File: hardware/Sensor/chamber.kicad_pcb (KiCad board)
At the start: 2 copper layers, 45 x 30 mm, 30 parts, among them J1 Power, J2 Chamber, J3 Output, Q1 Q_NJFET_DGS, Q2 BC546, Q3 BC327, U1 LMC6082

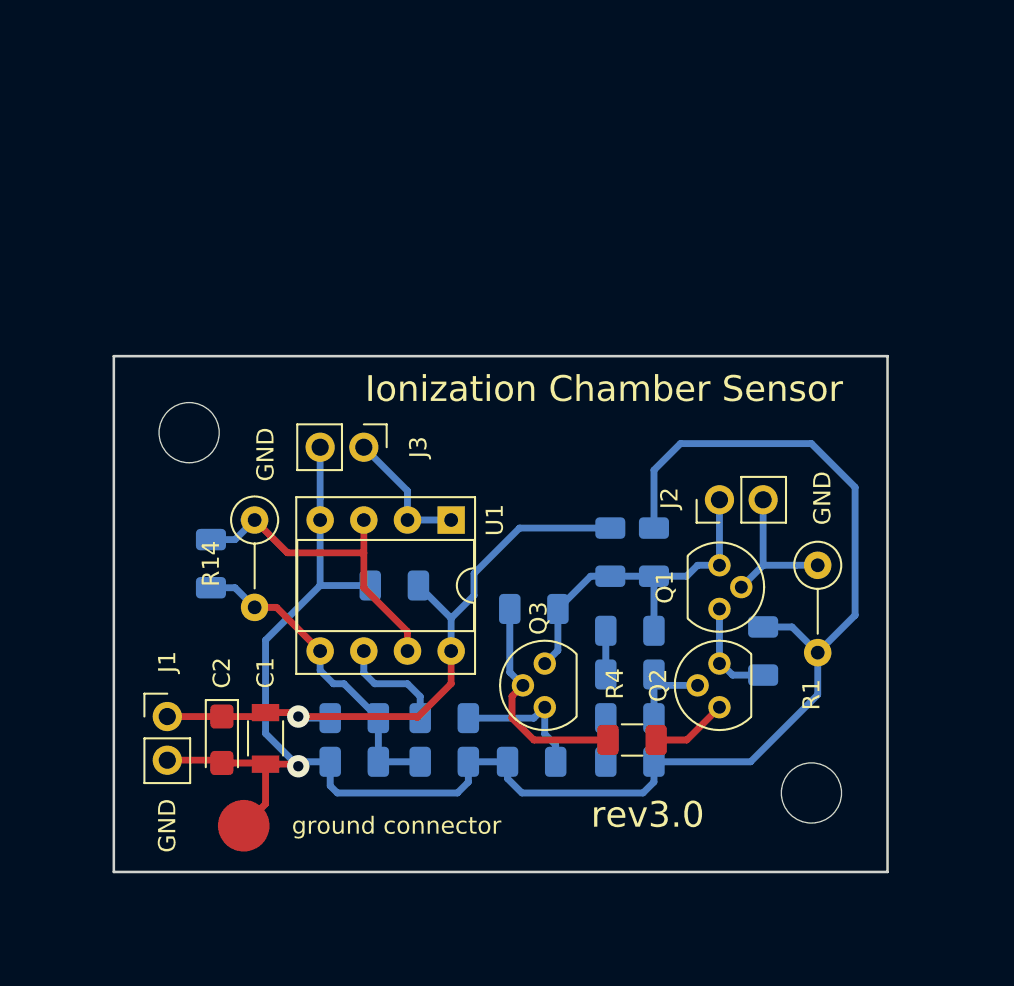
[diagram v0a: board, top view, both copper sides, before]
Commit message: fixed footprints
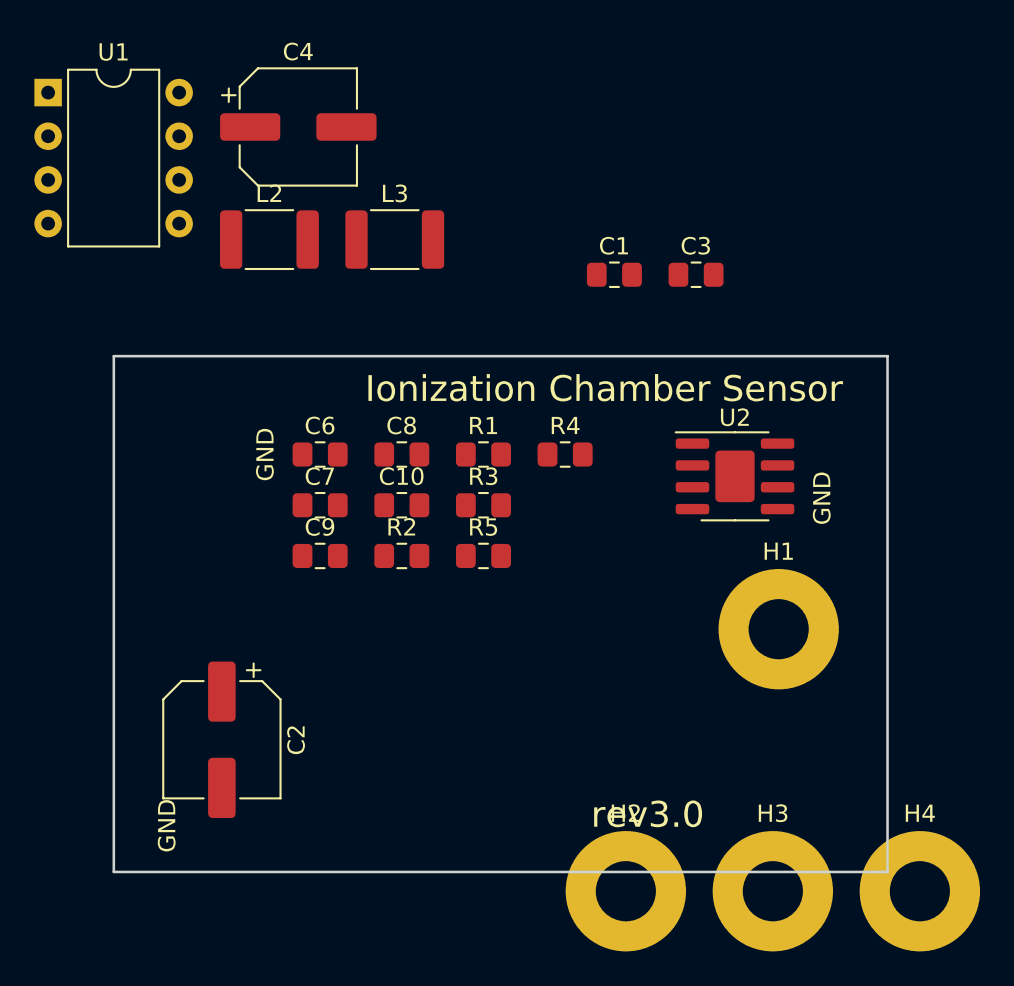
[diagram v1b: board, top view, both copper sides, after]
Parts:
- removed C5: 100n, Capacitor_SMD:C_1206_3216Metric
- removed J1: Power, Connector_PinHeader_2.54mm:PinHeader_1x02_P2.54mm_Vertical
- removed J2: Chamber, Connector_PinHeader_2.54mm:PinHeader_1x02_P2.54mm_Vertical
- removed J3: Output, Connector_PinHeader_2.54mm:PinHeader_1x02_P2.54mm_Vertical
- removed Q1: Q_NJFET_DGS, Package_TO_SOT_THT:TO-92
- removed Q2: BC546, Package_TO_SOT_THT:TO-92
- removed Q3: BC327, Package_TO_SOT_THT:TO-92
- removed R10: 1k, Resistor_SMD:R_1206_3216Metric
- removed R11: 47k, Resistor_SMD:R_1206_3216Metric
- removed R12, R13: R, Resistor_SMD:R_1206_3216Metric
- removed R14: 4M7, Resistor_THT:R_Axial_DIN0207_L6.3mm_D2.5mm_P5.08mm_Vertical
- removed R6, R7: 0R, Resistor_SMD:R_1206_3216Metric
- removed R8: 150k, Resistor_SMD:R_1206_3216Metric
- removed R9: 220k, Resistor_SMD:R_1206_3216Metric
- removed REF** (x2): MountingHole_3.5mm, Mounting_Holes:MountingHole_3.5mm
- removed ground connector: Measurement_Point_Round-SMD-Pad_Big, Measurement_Points:Measurement_Point_Round-SMD-Pad_Big
- added C10: 100n, Capacitor_SMD:C_0805_2012Metric_Pad1.15x1.40mm_HandSolder, F.Cu at (131.8, 48.7)
- added C7: 100n, Capacitor_SMD:C_0805_2012Metric_Pad1.15x1.40mm_HandSolder, F.Cu at (127.0, 48.7)
- added C8: 100n, Capacitor_SMD:C_0805_2012Metric_Pad1.15x1.40mm_HandSolder, F.Cu at (131.8, 45.7)
- added C9: 100n, Capacitor_SMD:C_0805_2012Metric_Pad1.15x1.40mm_HandSolder, F.Cu at (127.0, 51.6)
- added H1: top left, MountingHole:MountingHole_3.5mm_Pad, F.Cu at (153.7, 55.9)
- added H2: bottom left, MountingHole:MountingHole_3.5mm_Pad, F.Cu at (144.8, 71.1)
- added H3: top right, MountingHole:MountingHole_3.5mm_Pad, F.Cu at (153.3, 71.1)
- added H4: bottom right, MountingHole:MountingHole_3.5mm_Pad, F.Cu at (161.9, 71.1)
- added L2: u68, Inductor_SMD:L_1812_4532Metric_Pad1.30x3.40mm_HandSolder, F.Cu at (124.0, 33.2)
- added L3: u68, Inductor_SMD:L_1812_4532Metric_Pad1.30x3.40mm_HandSolder, F.Cu at (131.3, 33.2)
- added U2: LM358, Package_SO:SOIC-8-1EP_3.9x4.9mm_P1.27mm_EP2.29x3mm, F.Cu at (151.1, 47.0)
- C1: value 100n -> 2p2; footprint Capacitors_SMD:C_1206 -> Capacitor_SMD:C_0805_2012Metric_Pad1.15x1.40mm_HandSolder
- C2: footprint Capacitor_Tantalum_SMD:CP_EIA-3216-18_Kemet-A -> Capacitor_SMD:CP_Elec_6.3x5.4
- C3: value 100n -> C; footprint Capacitor_SMD:C_1206_3216Metric -> Capacitor_SMD:C_0805_2012Metric_Pad1.15x1.40mm_HandSolder; moved to F.Cu
- C4: value C -> 100u/16V; footprint Capacitor_SMD:C_1206_3216Metric -> Capacitor_SMD:CP_Elec_6.3x5.4; moved to F.Cu
- C6: footprint Capacitor_SMD:C_1206_3216Metric -> Capacitor_SMD:C_0805_2012Metric_Pad1.15x1.40mm_HandSolder; moved to F.Cu
- R1: value 1G -> 4*100G; footprint Resistor_THT:R_Axial_DIN0207_L6.3mm_D2.5mm_P5.08mm_Vertical -> Resistor_SMD:R_0805_2012Metric_Pad1.15x1.40mm_HandSolder
- R2: value 270k -> R; footprint Resistor_SMD:R_1206_3216Metric -> Resistor_SMD:R_0805_2012Metric_Pad1.15x1.40mm_HandSolder; moved to F.Cu
- R3: value 100k -> R; footprint Resistor_SMD:R_1206_3216Metric -> Resistor_SMD:R_0805_2012Metric_Pad1.15x1.40mm_HandSolder; moved to F.Cu
- R4: value 270k -> R; footprint Resistor_SMD:R_1206_3216Metric -> Resistor_SMD:R_0805_2012Metric_Pad1.15x1.40mm_HandSolder
- R5: value 47k -> R; footprint Resistor_SMD:R_1206_3216Metric -> Resistor_SMD:R_0805_2012Metric_Pad1.15x1.40mm_HandSolder; moved to F.Cu
- U1: value LMC6082 -> LMC662; footprint Housings_DIP:DIP-8_W7.62mm_Socket -> Package_DIP:DIP-8_W7.62mm
- moved C4 37.9 mm to (125.7, 26.7)
- moved U1 34.2 mm to (111.2, 24.7), turned to 0 degrees
- moved C1 33.7 mm to (144.1, 35.3), turned to 0 degrees
- moved R2 21.7 mm to (131.8, 51.6), turned to 0 degrees
- moved R1 20.5 mm to (136.5, 45.7), turned to 0 degrees
- moved R4 17.1 mm to (141.2, 45.7)
- moved C3 16.3 mm to (148.9, 35.3), turned to 0 degrees
- moved R5 9.56 mm to (136.5, 51.6), turned to 0 degrees
- moved C6 8.76 mm to (127.0, 45.7), turned to 0 degrees
- moved R3 6.71 mm to (136.5, 48.7), turned to 0 degrees
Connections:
- C1 pad 2: GND -> Net-(C1-Pad2)
- C2 pad 1: Net-(C1-Pad1) -> Net-(C2-Pad1)
- C6 pad 1: Net-(C1-Pad1) -> (no net)
- R1 pad 1: Net-(J2-Pad2) -> Net-(C1-Pad1)
- R1 pad 2: GND -> Net-(C1-Pad2)
- R2 pad 1: Net-(Q1-Pad3) -> Net-(R2-Pad1)
- R2 pad 2: GND -> Net-(C3-Pad1)
- R3 pad 1: Net-(C3-Pad1) -> Net-(R3-Pad1)
- R3 pad 2: Net-(Q3-Pad2) -> Net-(R2-Pad1)
- R4 pad 1: Net-(Q3-Pad2) -> Net-(R4-Pad1)
- R4 pad 2: Net-(Q2-Pad1) -> Net-(R3-Pad1)
- R5 pad 1: Net-(C3-Pad1) -> Net-(R5-Pad1)
- R5 pad 2: Net-(R5-Pad2) -> Net-(R4-Pad1)
- U1 pad 1: Net-(J3-Pad1) -> Net-(C1-Pad1)
- U1 pad 2: Net-(J3-Pad1) -> Net-(C1-Pad2)
- U1 pad 3: Net-(C5-Pad1) -> (no net)
- U1 pad 4: GND -> -6V
- U1 pad 5: Net-(C4-Pad1) -> Net-(C1-Pad1)
- U1 pad 6: Net-(R11-Pad1) -> Net-(R2-Pad1)
- U1 pad 7: Net-(C5-Pad1) -> Net-(R3-Pad1)
- U1 pad 8: Net-(C1-Pad1) -> +6V
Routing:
- net GND: track 107.5 -> 0.00 mm, vias 1 -> 0
- net Net-(C1-Pad1): track 38.3 -> 0.00 mm, vias 1 -> 0
- net Net-(C3-Pad1): track 20.9 -> 0.00 mm
- net Net-(C5-Pad1): track 19.7 -> 0.00 mm
- net Net-(C4-Pad1): track 19.2 -> 0.00 mm
- net Net-(Q3-Pad2): track 13.0 -> 0.00 mm
- net Net-(J2-Pad2): track 8.78 -> 0.00 mm
- net Net-(Q3-Pad1): track 8.15 -> 0.00 mm
- net Net-(J3-Pad1): track 7.83 -> 0.00 mm
- net Net-(R11-Pad1): track 7.00 -> 0.00 mm
- net Net-(Q1-Pad3): track 5.99 -> 0.00 mm
- net Net-(Q2-Pad2): track 5.34 -> 0.00 mm
- net Net-(Q2-Pad1): track 4.47 -> 0.00 mm
- net Net-(R5-Pad2): track 2.54 -> 0.00 mm
- net Net-(R7-Pad2): track 2.54 -> 0.00 mm

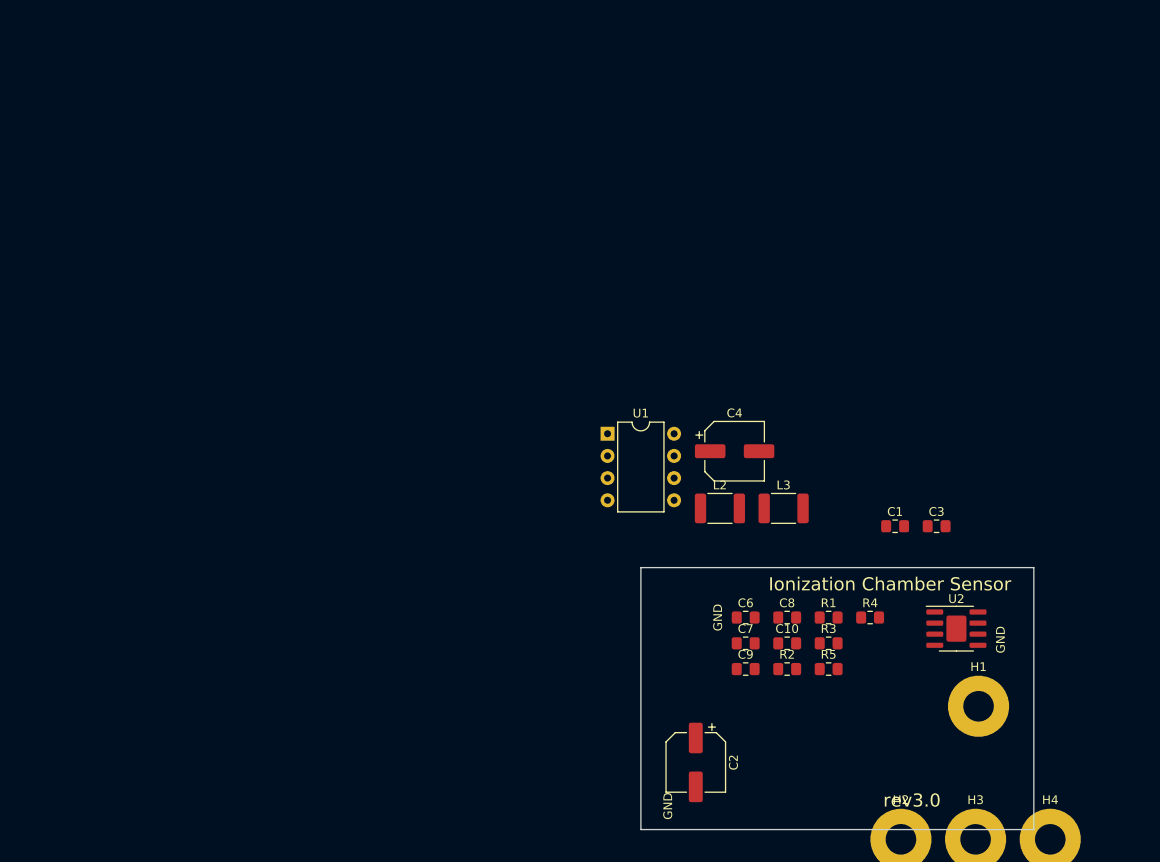
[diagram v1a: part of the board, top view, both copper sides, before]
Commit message: hw converter added
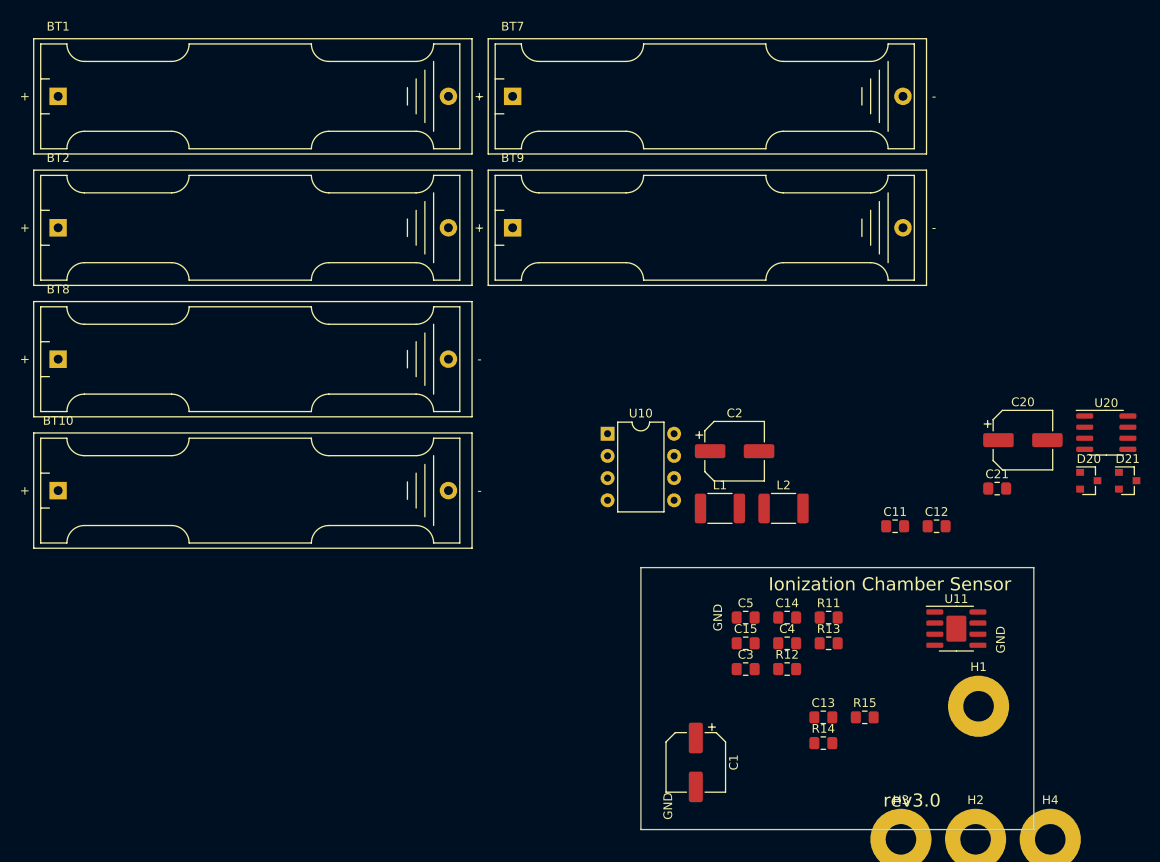
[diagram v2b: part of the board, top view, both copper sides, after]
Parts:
- removed R4, R5: R, Resistor_SMD:R_0805_2012Metric_Pad1.15x1.40mm_HandSolder
- added BT1: 1V5, Battery:BatteryHolder_Keystone_2466_1xAAA, F.Cu at (48.3, -14.0)
- added BT10: 1V5, Battery:BatteryHolder_Keystone_2466_1xAAA, F.Cu at (48.3, 31.2)
- added BT2: 1V5, Battery:BatteryHolder_Keystone_2466_1xAAA, F.Cu at (48.3, 1.08)
- added BT7: 1V5, Battery:BatteryHolder_Keystone_2466_1xAAA, F.Cu at (100.3, -14.0)
- added BT8: 1V5, Battery:BatteryHolder_Keystone_2466_1xAAA, F.Cu at (48.3, 16.1)
- added BT9: 1V5, Battery:BatteryHolder_Keystone_2466_1xAAA, F.Cu at (100.3, 1.08)
- added C13: C, Capacitor_SMD:C_0805_2012Metric_Pad1.15x1.40mm_HandSolder, F.Cu at (135.9, 57.1)
- added C20: 10u/16V, Capacitor_SMD:CP_Elec_6.3x5.4, F.Cu at (158.8, 25.4)
- added C21: 100n, Capacitor_SMD:C_0805_2012Metric_Pad1.15x1.40mm_HandSolder, F.Cu at (155.8, 30.9)
- added D20: D_Schottky, Diode_SMD:D_SOT-23_ANK, F.Cu at (166.3, 30.1)
- added D21: D_Schottky, Diode_SMD:D_SOT-23_ANK, F.Cu at (170.8, 30.1)
- added R14: R, Resistor_SMD:R_0805_2012Metric_Pad1.15x1.40mm_HandSolder, F.Cu at (135.9, 60.1)
- added R15: R, Resistor_SMD:R_0805_2012Metric_Pad1.15x1.40mm_HandSolder, F.Cu at (140.6, 57.1)
- added U20: ICL7660, Package_SO:SOIC-8_3.9x4.9mm_P1.27mm, F.Cu at (168.3, 24.6)
- renumbered C2 to C1, C1 to C11, C3 to C12, C8 to C14, C7 to C15, C4 to C2, C9 to C3, C10 to C4, C6 to C5, H3 to H2, H2 to H3, L2 to L1, L3 to L2, R1 to R11, R2 to R12, R3 to R13, U1 to U10, U2 to U11
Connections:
- net +6V renamed +BATT
- net -6V renamed -BATT
- R13 pad 1: Net-(R3-Pad1) -> Net-(R13-Pad1)
- U10 pad 3: (no net) -> GND
- U10 pad 7: Net-(R3-Pad1) -> Net-(R13-Pad1)
- U11 pad 3: GND -> Net-(R13-Pad1)

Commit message: sensor + high voltage schemat
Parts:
- removed C5: 100n, Capacitor_SMD:C_0805_2012Metric_Pad1.15x1.40mm_HandSolder
- added C22: 10n, Capacitor_SMD:C_0805_2012Metric_Pad1.15x1.40mm_HandSolder, F.Cu at (67.4, 60.2)
- added C23: 10n/600V, Capacitor_SMD:C_0805_2012Metric_Pad1.15x1.40mm_HandSolder, F.Cu at (43.2, 48.3)
- added C24: 10n/600V, Capacitor_SMD:C_0805_2012Metric_Pad1.15x1.40mm_HandSolder, F.Cu at (47.9, 48.3)
- added D22: 1N4007, Diode_THT:D_DO-41_SOD81_P10.16mm_Horizontal, F.Cu at (48.3, 55.9)
- added D23: 1N4007, Diode_THT:D_DO-41_SOD81_P10.16mm_Horizontal, F.Cu at (62.2, 64.8)
- added J10: Conn_Coaxial, Connector_Coaxial:SMA_Molex_73251-1153_EdgeMount_Horizontal, F.Cu at (156.2, 29.2)
- added JP20: close(1) = disable HV gen, Jumper:SolderJumper-2_P1.3mm_Open_Pad1.0x1.5mm, F.Cu at (78.7, 61.0)
- added L20: 680m, Inductor_THT:L_Radial_L8.0mm_W8.0mm_P5.00mm_Neosid_NE-CPB-07E, F.Cu at (105.4, 64.8)
- added Q20: BC859, Package_TO_SOT_SMD:SOT-23, F.Cu at (85.9, 53.3)
- added Q21: Q_NMOS_GDS, Package_TO_SOT_THT:TO-220-3_Horizontal_TabUp, F.Cu at (93.5, 56.7)
- added R20: R22/0.5W, Resistor_THT:R_Axial_DIN0207_L6.3mm_D2.5mm_P5.08mm_Vertical, F.Cu at (81.3, 52.5)
- added R21: 10k, Resistor_SMD:R_0805_2012Metric_Pad1.15x1.40mm_HandSolder, F.Cu at (72.1, 60.2)
- added R22: 10M, Resistor_THT:R_Axial_DIN0207_L6.3mm_D2.5mm_P10.16mm_Horizontal, F.Cu at (75.8, 56.7)
- added R23: 1k, Resistor_SMD:R_0805_2012Metric_Pad1.15x1.40mm_HandSolder, F.Cu at (86.0, 49.5)
- added R24: 30k, Resistor_SMD:R_0805_2012Metric_Pad1.15x1.40mm_HandSolder, F.Cu at (80.6, 55.4)
- added R25: 10M, Resistor_THT:R_Axial_DIN0207_L6.3mm_D2.5mm_P10.16mm_Horizontal, F.Cu at (42.4, 44.8)
- C20: value 10u/16V -> 3n2; footprint Capacitor_SMD:CP_Elec_6.3x5.4 -> Capacitor_SMD:C_0805_2012Metric_Pad1.15x1.40mm_HandSolder
- D20: value D_Schottky -> 1N4007; footprint Diode_SMD:D_SOT-23_ANK -> Diode_THT:D_DO-41_SOD81_P10.16mm_Horizontal
- U20: value ICL7660 -> MC34063AD
- moved D21 119.7 mm to (52.5, 49.1)
- moved U20 103.8 mm to (69.2, 55.5)
- moved D20 101.4 mm to (66.9, 50.2)
- moved C21 83.2 mm to (75.8, 53.8)
- moved C20 81.1 mm to (81.3, 49.5)
- moved C1 44.5 mm to (121.9, 17.8)
- moved H1 22.2 mm to (133.3, 64.8)
- moved U10 18.5 mm to (111.8, 43.2)
- moved C2 17.3 mm to (109.2, 21.6)
- moved L2 17.3 mm to (114.8, 28.1)
- moved L1 17.3 mm to (107.5, 28.1)
- moved R14 8.71 mm to (128.3, 55.9)
- moved H2 7.63 mm to (153.7, 63.5)
- moved H4 6.39 mm to (162.6, 64.8)
- moved H3 6.35 mm to (144.8, 64.8)
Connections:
- C20 pad 2: Net-(C20-Pad2) -> GND
- C21 pad 1: (no net) -> GND
- C21 pad 2: (no net) -> +BATT
- D20 pad 1: Net-(C20-Pad2) -> Net-(C23-Pad1)
- D21 pad 1: (no net) -> Net-(D21-Pad1)
- D21 pad 2: (no net) -> Net-(D21-Pad2)
- U20 pad 1: (no net) -> Net-(L20-Pad1)
- U20 pad 2: Net-(C20-Pad1) -> Net-(D21-Pad2)
- U20 pad 3: -BATT -> Net-(C20-Pad1)
- U20 pad 4: (no net) -> GND
- U20 pad 5: -BATT -> Net-(C22-Pad1)
- U20 pad 6: (no net) -> +BATT
- U20 pad 7: (no net) -> Net-(L20-Pad1)
- U20 pad 8: Net-(D20-Pad2) -> Net-(L20-Pad1)
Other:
- board outline removed

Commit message: changed power source
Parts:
- moved L20 151.9 mm to (-37.6, 115.8)
- moved Q21 151.9 mm to (-49.5, 107.7)
- moved BT7 105.0 mm to (7.83, 35.8)
- moved BT1 104.7 mm to (-44.0, 35.5)
- moved C1 100.8 mm to (41.9, 79.0)
- moved J10 99.8 mm to (69.5, 78.7)
- moved R14 99.8 mm to (41.6, 105.4)
- moved BT10 99.8 mm to (-38.4, 80.7)
- moved BT2 99.8 mm to (-38.4, 50.6)
- moved BT8 99.8 mm to (-38.4, 65.6)
- moved BT9 99.8 mm to (13.7, 50.6)
- moved C11 99.8 mm to (57.5, 84.8)
- moved C12 99.8 mm to (62.2, 84.8)
- moved C13 99.8 mm to (49.2, 106.7)
- moved C14 99.8 mm to (45.1, 95.2)
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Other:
- board outline added: 100 x 100 mm

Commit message: draft of digital part
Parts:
- removed BT10, BT7, BT8, BT9: 1V5, Battery:BatteryHolder_Keystone_2466_1xAAA
- added C30: 100n, Capacitor_SMD:C_0805_2012Metric_Pad1.15x1.40mm_HandSolder, F.Cu at (50.0, 45.0)
- added C31: 100n, Capacitor_SMD:C_0805_2012Metric_Pad1.15x1.40mm_HandSolder, F.Cu at (50.0, 48.0)
- added C32: 100n, Capacitor_SMD:C_0805_2012Metric_Pad1.15x1.40mm_HandSolder, F.Cu at (54.8, 45.0)
- added C5: 100u/16V, Capacitor_SMD:CP_Elec_6.3x5.4, F.Cu at (-20.0, 135.0)
- added C6: 100u/16V, Capacitor_SMD:CP_Elec_6.3x5.4, F.Cu at (-7.85, 127.0)
- added R26: 10M, Resistor_THT:R_Axial_DIN0207_L6.3mm_D2.5mm_P10.16mm_Horizontal, F.Cu at (-20.0, 95.0)
- added U1: L7805, Package_TO_SOT_SMD:TO-252-2, F.Cu at (-19.2, 126.9)
- added U30: STM32F070F6Px, Package_SO:TSSOP-20_4.4x6.5mm_P0.65mm, F.Cu at (50.0, 55.0)
- added U31: MCP3425A0T-ECH, Package_TO_SOT_SMD:SOT-23-6_Handsoldering, F.Cu at (65.0, 50.0)
- BT1, BT2: value 1V5 -> 2 x 3V6
- moved BT1 197.2 mm to (152.5, 53.0), turned to 180 degrees
- moved BT2 156.3 mm to (116.6, 70.6)
- moved J10 10.3 mm to (71.1, 68.6)
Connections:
- BT1 pad 1: Net-(BT1-Pad1) -> (no net)
- BT2 pad 1: Net-(BT2-Pad1) -> (no net)
- C21 pad 2: +BATT -> +5V
- D23 pad 2: +BATT -> +5V
- R20 pad 1: +BATT -> +5V
- R25 pad 1: Net-(D22-Pad1) -> Net-(R25-Pad1)
- U20 pad 6: +BATT -> +5V

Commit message: added footprints
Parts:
- added J10: RF_Shield_Two_Pieces, IonizationChamber:IonizationChamberShield, F.Cu at (10.3, 57.1)
- added J20: RF_Shield_Two_Pieces, IonizationChamber:IonizationChamberHVShield, F.Cu at (11.6, 97.8)
- added V10: Nuclear-Radiation_Detector, IonizationChamber:IonizationChamberSensor, B.Cu at (49.7, 46.9)
- moved BT1 122.4 mm to (38.3, 8.89), turned to 270 degrees
- moved C2 105.7 mm to (108.1, 8.89)
- moved H4 100.1 mm to (3.71, 5.08)
- moved H1 98.0 mm to (6.21, 94.4)
- moved H2 98.0 mm to (93.7, 94.4)
- moved C1 97.4 mm to (115.7, 15.5)
- moved C13 97.4 mm to (123.0, 43.2)
- moved R15 97.4 mm to (127.8, 43.2)
- moved U10 97.4 mm to (98.9, 29.2)
- moved C15 97.4 mm to (114.2, 34.7)
- moved C4 97.4 mm to (118.9, 34.7)
- moved R13 97.4 mm to (123.7, 34.7)
- moved C11 97.4 mm to (131.3, 21.3)
- moved C12 97.4 mm to (136.0, 21.3)
- moved C14 97.4 mm to (118.9, 31.7)
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- renumbered J10 to J11
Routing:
- net Net-(D22-Pad1): track 0.00 -> 52.3 mm
- added copper zone on B.Cu, net GND
- added copper zone on F.Cu, net GND
